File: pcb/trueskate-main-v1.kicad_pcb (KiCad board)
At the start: 2 copper layers, 160 x 120 mm, 51 parts, among them J1 Teensy 4.1 FEMALE 1x24, J11 Mini v1.0 / 15-hole socket, J12 Mini v1.0 / 15-hole socket, J13 Mini v1.0 / 15-hole socket, J14 Mini v1.0 / 15-hole socket, J15 Mini v1.0 / 15-hole socket, J16 Mini v1.0 / 15-hole socket, J2 Teensy 4.1 FEMALE 1x24, J21 MOTOR PHASES male 1x3, J22 MOTOR PHASES male 1x3, J23 MOTOR PHASES male 1x3, J24 MOTOR PHASES male 1x3, J25 MOTOR PHASES male 1x3, J26 MOTOR PHASES male 1x3, J31 ENCODER breakout FEMALE 1x6, J32 ENCODER breakout FEMALE 1x6, J33 ENCODER breakout FEMALE 1x6, J34 ENCODER breakout FEMALE 1x6, J35 ENCODER breakout FEMALE 1x6, J36 ENCODER breakout FEMALE 1x6, J5 12V INPUT + / -

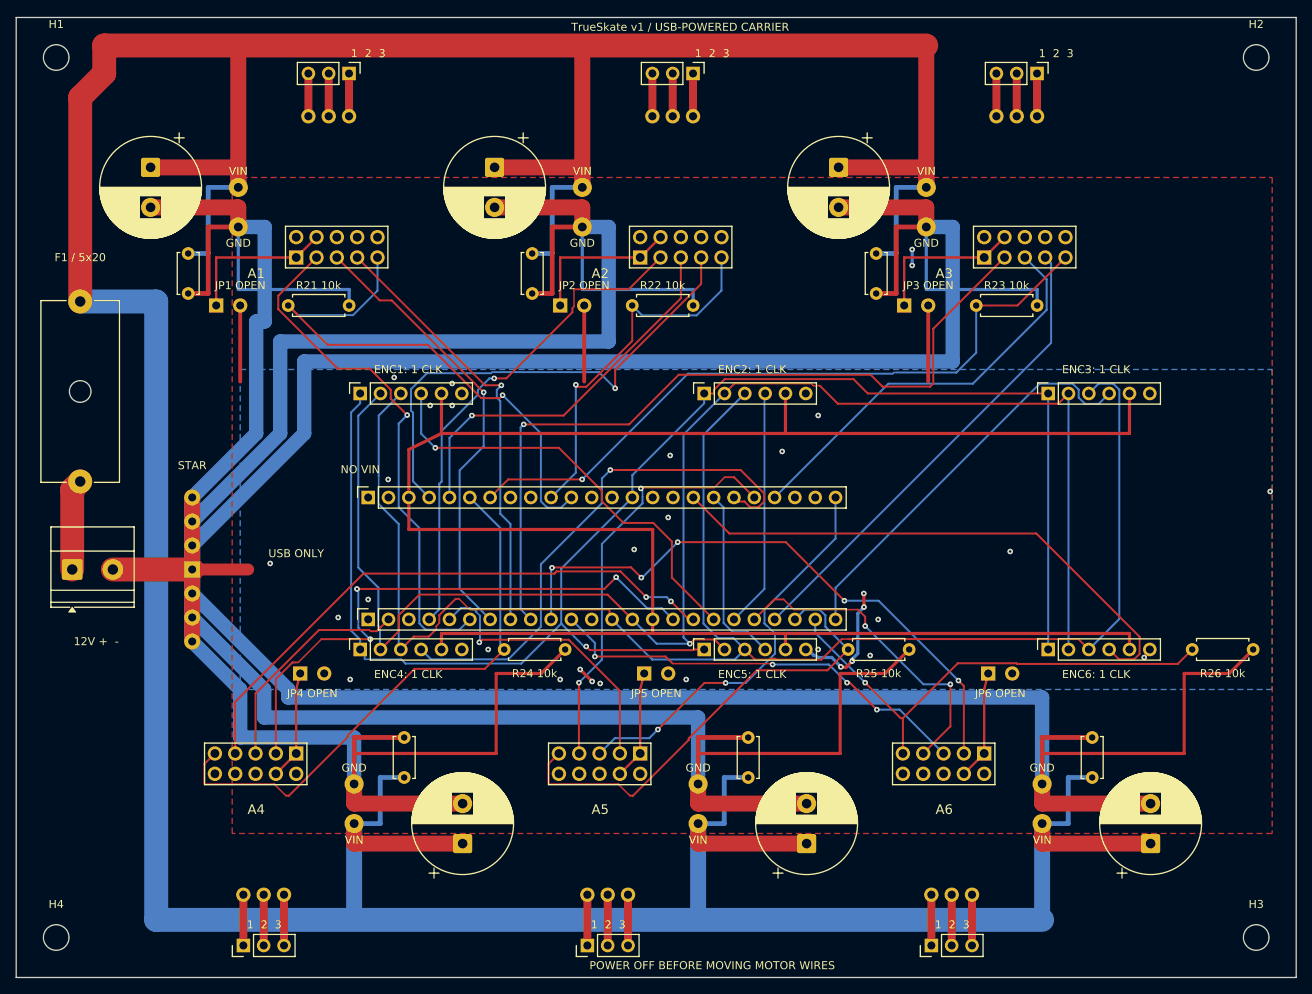
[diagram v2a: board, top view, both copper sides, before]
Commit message: feat: relayout carrier with edge connectors and hardware kill
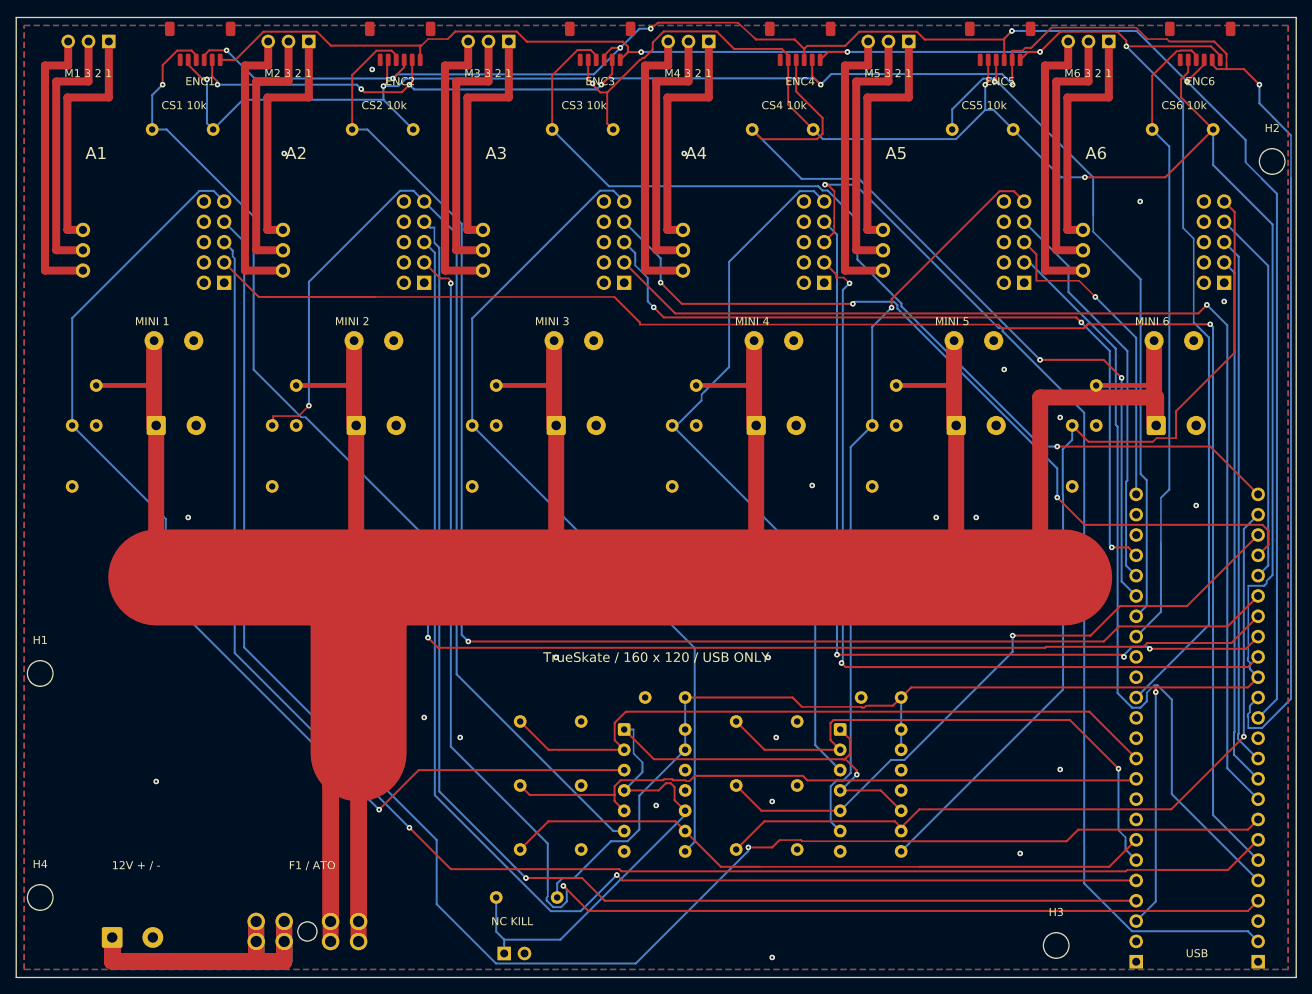
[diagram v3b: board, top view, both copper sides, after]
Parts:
- removed JP1, JP2, JP3, JP4, JP5, JP6: CONTROL GND / OPEN, TrueSkate:GroundBridge_THT
- removed NT1: GROUND STAR / PCB COPPER, TrueSkate:GroundStar
- added C1: 100nF buffer bypass, TrueSkate:Edge_C_Disc_D5.0mm_W2.5mm_P5.00mm, F.Cu at (83.6, 85.0)
- added C2: 100nF buffer bypass, TrueSkate:Edge_C_Disc_D5.0mm_W2.5mm_P5.00mm, F.Cu at (110.6, 85.0)
- added J6: NC KILL SWITCH, TrueSkate:Edge_PinHeader_1x02_P2.54mm_Vertical, F.Cu at (61.0, 117.0)
- added R1: 10k /OE pull-up, TrueSkate:Edge_R_Axial_DIN0207_L6.3mm_D2.5mm_P7.62mm_Horizontal, F.Cu at (60.0, 110.0)
- added R31: 10k CS pull-up, TrueSkate:Edge_R_Axial_DIN0207_L6.3mm_D2.5mm_P7.62mm_Horizontal, F.Cu at (17.0, 14.0)
- added R32: 10k CS pull-up, TrueSkate:Edge_R_Axial_DIN0207_L6.3mm_D2.5mm_P7.62mm_Horizontal, F.Cu at (42.0, 14.0)
- added R33: 10k CS pull-up, TrueSkate:Edge_R_Axial_DIN0207_L6.3mm_D2.5mm_P7.62mm_Horizontal, F.Cu at (67.0, 14.0)
- added R34: 10k CS pull-up, TrueSkate:Edge_R_Axial_DIN0207_L6.3mm_D2.5mm_P7.62mm_Horizontal, F.Cu at (92.0, 14.0)
- added R35: 10k CS pull-up, TrueSkate:Edge_R_Axial_DIN0207_L6.3mm_D2.5mm_P7.62mm_Horizontal, F.Cu at (117.0, 14.0)
- added R36: 10k CS pull-up, TrueSkate:Edge_R_Axial_DIN0207_L6.3mm_D2.5mm_P7.62mm_Horizontal, F.Cu at (142.0, 14.0)
- added R41: 10k EN command pull-down, TrueSkate:Edge_R_Axial_DIN0207_L6.3mm_D2.5mm_P7.62mm_Horizontal, F.Cu at (63.0, 88.0)
- added R42: 10k EN command pull-down, TrueSkate:Edge_R_Axial_DIN0207_L6.3mm_D2.5mm_P7.62mm_Horizontal, F.Cu at (63.0, 96.0)
- added R43: 10k EN command pull-down, TrueSkate:Edge_R_Axial_DIN0207_L6.3mm_D2.5mm_P7.62mm_Horizontal, F.Cu at (63.0, 104.0)
- added R44: 10k EN command pull-down, TrueSkate:Edge_R_Axial_DIN0207_L6.3mm_D2.5mm_P7.62mm_Horizontal, F.Cu at (90.0, 88.0)
- added R45: 10k EN command pull-down, TrueSkate:Edge_R_Axial_DIN0207_L6.3mm_D2.5mm_P7.62mm_Horizontal, F.Cu at (90.0, 96.0)
- added R46: 10k EN command pull-down, TrueSkate:Edge_R_Axial_DIN0207_L6.3mm_D2.5mm_P7.62mm_Horizontal, F.Cu at (90.0, 104.0)
- added U1: SN74LV125AN, TrueSkate:Edge_DIP-14_W7.62mm, F.Cu at (76.0, 89.0)
- added U2: SN74LV125AN, TrueSkate:Edge_DIP-14_W7.62mm, F.Cu at (103.0, 89.0)
- C11, C12, C13, C14, C15, C16: footprint Capacitor_THT:CP_Radial_D12.5mm_P5.00mm -> TrueSkate:Edge_CP_Radial_D12.5mm_P5.00mm
- C21, C22, C23, C24, C25, C26: footprint Capacitor_THT:C_Disc_D5.0mm_W2.5mm_P5.00mm -> TrueSkate:Edge_C_Disc_D5.0mm_W2.5mm_P5.00mm
- F1: value 5x20 fuse holder / fuse TBD -> ATO fuse holder / fuse TBD; footprint Fuse:Fuseholder_Cylinder-5x20mm_Schurter_0031_8201_Horizontal_Open -> TrueSkate:Edge_FuseHolder_Blade_ATO_Littelfuse_FLR_178.6165
- J1, J2: footprint Connector_PinSocket_2.54mm:PinSocket_1x24_P2.54mm_Vertical -> TrueSkate:Edge_PinSocket_1x24_P2.54mm_Vertical
- J21, J22, J23, J24, J25, J26: footprint Connector_PinHeader_2.54mm:PinHeader_1x03_P2.54mm_Vertical -> TrueSkate:Edge_PinHeader_1x03_P2.54mm_Vertical
- J31, J32, J33, J34, J35, J36: value ENCODER breakout FEMALE 1x6 -> SM06B-SRSS-TB; footprint Connector_PinSocket_2.54mm:PinSocket_1x06_P2.54mm_Vertical -> TrueSkate:Edge_JST_SH_SM06B-SRSS-TB_1x06-1MP_P1.00mm_Horizontal
- J5: footprint TerminalBlock_Phoenix:TerminalBlock_Phoenix_MKDS-1,5-2-5.08_1x02_P5.08mm_Horizontal -> TrueSkate:Edge_TerminalBlock_Phoenix_MKDS-1,5-2-5.08_1x02_P5.08mm_Horizontal
- R21, R22, R23, R24, R25, R26: footprint Resistor_THT:R_Axial_DIN0207_L6.3mm_D2.5mm_P7.62mm_Horizontal -> TrueSkate:Edge_R_Axial_DIN0207_L6.3mm_D2.5mm_P7.62mm_Horizontal
- moved J24 127.1 mm to (86.6, 3.00), turned to -90 degrees
- moved J25 119.9 mm to (111.6, 3.00), turned to -90 degrees
- moved J1 119.2 mm to (155.2, 118.0), turned to 180 degrees
- moved J26 115.2 mm to (136.6, 3.00), turned to -90 degrees
- moved J2 112.2 mm to (140.0, 118.0), turned to 180 degrees
- moved J14 102.8 mm to (101.0, 23.0), turned to -90 degrees
- moved J34 93.6 mm to (98.0, 3.30), turned to 180 degrees
- moved J15 90.2 mm to (126.0, 23.0), turned to -90 degrees
- moved J35 84.3 mm to (123.0, 3.30), turned to 180 degrees
- moved J16 79.8 mm to (151.0, 23.0), turned to -90 degrees
- moved J36 78.0 mm to (148.0, 3.30), turned to 180 degrees
- moved H1 77.0 mm to (3.00, 82.0)
- moved J33 71.0 mm to (73.0, 3.30), turned to 180 degrees
- moved J23 66.1 mm to (61.6, 3.00)
- moved R23 64.8 mm to (57.0, 51.0), turned to -90 degrees
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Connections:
- C11 pad 2: PGND1 -> GND
- C12 pad 2: PGND2 -> GND
- C13 pad 2: PGND3 -> GND
- C14 pad 2: PGND4 -> GND
- C15 pad 2: PGND5 -> GND
- C16 pad 2: PGND6 -> GND
- C21 pad 2: PGND1 -> GND
- C22 pad 2: PGND2 -> GND
- C23 pad 2: PGND3 -> GND
- C24 pad 2: PGND4 -> GND
- C25 pad 2: PGND5 -> GND
- C26 pad 2: PGND6 -> GND
- J1 pad 22: A5_EN -> A5_EN_CMD
- J1 pad 23: A6_EN -> A6_EN_CMD
- J11 pad 1: CGND1 -> GND
- J11 pad 4: CGND1 -> GND
- J11 pad GND: PGND1 -> GND
- J12 pad 1: CGND2 -> GND
- J12 pad 4: CGND2 -> GND
- J12 pad GND: PGND2 -> GND
- J13 pad 1: CGND3 -> GND
- J13 pad 4: CGND3 -> GND
- J13 pad GND: PGND3 -> GND
- J14 pad 1: CGND4 -> GND
- J14 pad 4: CGND4 -> GND
- J14 pad GND: PGND4 -> GND
- J15 pad 1: CGND5 -> GND
- J15 pad 4: CGND5 -> GND
- J15 pad GND: PGND5 -> GND
- J16 pad 1: CGND6 -> GND
- J16 pad 4: CGND6 -> GND
- J16 pad GND: PGND6 -> GND
- J2 pad 10: A2_EN -> A2_EN_CMD
- J2 pad 11: A1_EN -> A1_EN_CMD
- J2 pad 6: A4_EN -> A4_EN_CMD
- J2 pad 7: A3_EN -> A3_EN_CMD
- R21 pad 2: PGND1 -> GND
- R22 pad 2: PGND2 -> GND
- R23 pad 2: PGND3 -> GND
- R24 pad 2: PGND4 -> GND
- R25 pad 2: PGND5 -> GND
- R26 pad 2: PGND6 -> GND
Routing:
- net 12V_IN: track 11.4 -> 212.0 mm
- net PGND6: track 192.5 -> 0.00 mm
- net PGND3: track 181.6 -> 0.00 mm
- net 3V3: track 251.0 -> 412.8 mm, vias 0 -> 6
- net A2_CS: track 29.9 -> 186.6 mm, vias 0 -> 1
- net A1_PWM3: track 54.8 -> 209.9 mm
- net PGND5: track 148.3 -> 0.00 mm
- net A1_CS: track 54.6 -> 199.5 mm, vias 1 -> 2
- net PGND2: track 137.4 -> 0.00 mm
- net A1_PWM2: track 56.5 -> 192.8 mm
- net A1_PWM1: track 65.4 -> 196.5 mm
- net A2_PWM1: track 62.5 -> 180.8 mm, vias 1 -> 2
- net A2_PWM2: track 48.7 -> 165.5 mm
- net A4_PWM2: track 28.1 -> 136.4 mm, vias 0 -> 1
- net EN_DISABLE: track 0.00 -> 105.4 mm, vias 0 -> 1
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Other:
- board text added: "12V + / -"
- board text added: "CS1 10k"
- board text added: "CS2 10k"
- board text added: "CS3 10k"
- board text added: "CS4 10k"
- board text added: "CS5 10k"
- board text added: "CS6 10k"
- board text added: "ENC1"
- board text added: "ENC2"
- board text added: "ENC3"
- board text added: "ENC4"
- board text added: "ENC5"
- board text added: "ENC6"
- board text added: "F1 / ATO"
- board text added: "M1 3 2 1"
- board text added: "M2 3 2 1"
- board text added: "M3 3 2 1"
- board text added: "M4 3 2 1"
- board text added: "M5 3 2 1"
- board text added: "M6 3 2 1"
- board text added: "MINI 1"
- board text added: "MINI 2"
- board text added: "MINI 3"
- board text added: "MINI 4"
- board text added: "MINI 5"
- board text added: "MINI 6"
- board text added: "NC KILL"
- board text added: "TrueSkate / 160 x 120 / USB ONLY"
- board text added: "USB"
- board text removed: "1 2 3"
- board text removed: "12V + -"
- board text removed: "ENC1: 1 CLK"
- board text removed: "ENC2: 1 CLK"
- board text removed: "ENC3: 1 CLK"
- board text removed: "ENC4: 1 CLK"
- board text removed: "ENC5: 1 CLK"
- board text removed: "ENC6: 1 CLK"
- board text removed: "F1 / 5x20"
- board text removed: "JP1 OPEN"
- board text removed: "JP2 OPEN"
- board text removed: "JP3 OPEN"
- board text removed: "JP4 OPEN"
- board text removed: "JP5 OPEN"
- board text removed: "JP6 OPEN"
- board text removed: "NO VIN"
- board text removed: "POWER OFF BEFORE MOVING MOTOR WIRES"
- board text removed: "R21 10k"
- board text removed: "R22 10k"
- board text removed: "R23 10k"
- board text removed: "R24 10k"
- board text removed: "R25 10k"
- board text removed: "R26 10k"
- board text removed: "STAR"
- board text removed: "TrueSkate v1 / USB-POWERED CARRIER"
- board text removed: "USB ONLY"

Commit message: fix: refine carrier clearances and routing with populated renders
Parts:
- F1: value ATO fuse holder / fuse TBD -> Keystone 3557-2 ATO holder; footprint TrueSkate:Edge_FuseHolder_Blade_ATO_Littelfuse_FLR_178.6165 -> TrueSkate:Keystone_3557-2_ATO
- moved R31 47.1 mm to (19.6, 61.0)
- moved R32 47.1 mm to (44.6, 61.0)
- moved R33 47.1 mm to (69.6, 61.0)
- moved R34 47.1 mm to (94.6, 61.0)
- moved R35 47.1 mm to (119.6, 61.0)
- moved R36 47.1 mm to (144.6, 61.0)
- moved C21 1.00 mm to (10.0, 47.0)
- moved C22 1.00 mm to (35.0, 47.0)
- moved C23 1.00 mm to (60.0, 47.0)
- moved C24 1.00 mm to (85.0, 47.0)
- moved C25 1.00 mm to (110.0, 47.0)
- moved C26 1.00 mm to (135.0, 47.0)
- moved C11 0.50 mm to (17.5, 51.5)
- moved C12 0.50 mm to (42.5, 51.5)
- moved C13 0.50 mm to (67.5, 51.5)
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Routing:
- net SPI_SCK: track 232.0 -> 591.7 mm, vias 4 -> 15
- net SPI_MISO: track 249.0 -> 545.3 mm, vias 7 -> 19
- net 3V3: track 412.8 -> 701.7 mm, vias 6 -> 4
- net SPI_MOSI: track 232.3 -> 494.3 mm, vias 6 -> 14
- net GND: track 0.00 -> 258.6 mm, vias 23 -> 41
- net 12V_IN: track 212.0 -> 99.2 mm
- net A3_PWM2: track 97.1 -> 149.1 mm, vias 3 -> 4
- net A3_CS: track 124.6 -> 175.6 mm
- net 12V_FUSED: track 504.8 -> 462.9 mm
- net A3_PWM3: track 104.5 -> 140.6 mm, vias 3 -> 2
- net A4_PWM2: track 136.4 -> 168.5 mm, vias 1 -> 5
- net A6_EN: track 109.3 -> 140.2 mm, vias 0 -> 1
- net A5_PWM2: track 40.5 -> 70.4 mm, vias 1 -> 3
- net A4_PWM3: track 108.9 -> 136.4 mm, vias 3 -> 4
- net A1_PWM2: track 192.8 -> 218.1 mm, vias 1 -> 5
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
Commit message: feat: convert carrier to four layers with dedicated power and ground planes
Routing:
- added copper zone on In2.Cu, net 12V_FUSED
- added copper zone on In2.Cu, net 12V_IN
- added copper zone on In1.Cu, net GND
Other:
- copper layers 2 -> 4

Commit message: feat: restore two-layer 1 oz carrier with ground stitching
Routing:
- net GND: vias 41 -> 347
- removed copper zone on In2.Cu, net 12V_FUSED
- removed copper zone on In2.Cu, net 12V_IN
- removed copper zone on In1.Cu, net GND
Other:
- copper layers 4 -> 2
